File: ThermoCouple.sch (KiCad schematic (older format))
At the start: 0 parts

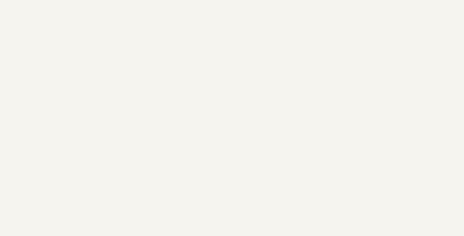
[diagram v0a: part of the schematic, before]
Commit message: create inputs and outputs for main modules
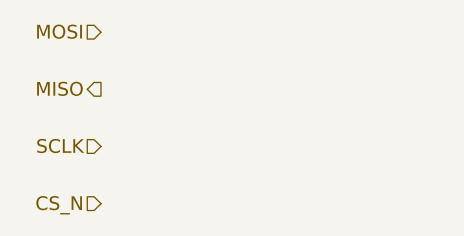
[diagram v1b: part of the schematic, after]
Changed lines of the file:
@@
 Text HLabel 8800 2900 0    60   Input ~ 0
 TC IN -
+Text HLabel 2850 2650 0    60   Input ~ 0
+MOSI
+Text HLabel 2850 2900 0    60   Output ~ 0
+MISO
+Text HLabel 2850 3150 0    60   Input ~ 0
+SCLK
+Text HLabel 2850 3400 0    60   Input ~ 0
+CS_N
 $EndSCHEMATC

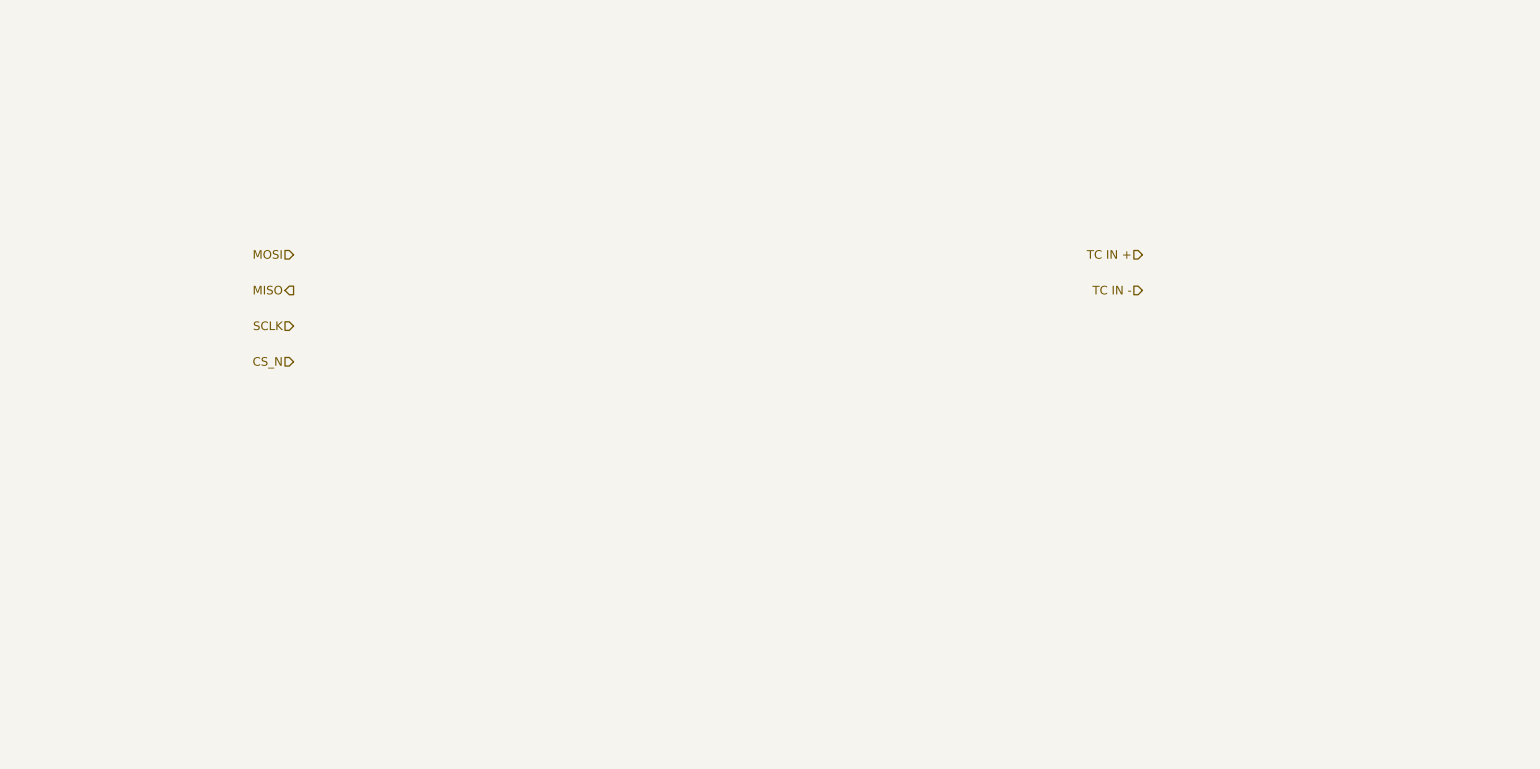
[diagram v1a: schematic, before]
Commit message: Added Start of thermocouple circuit
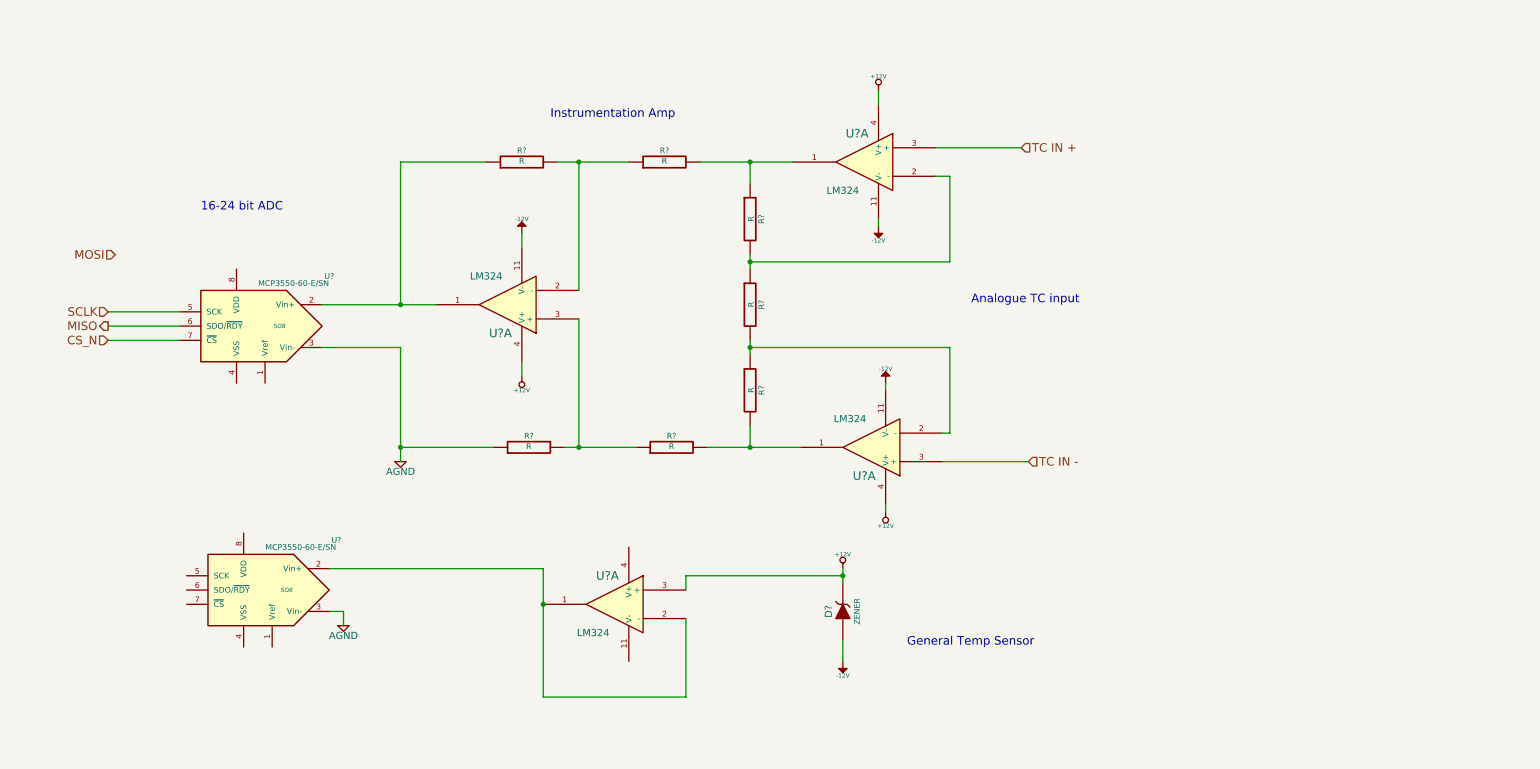
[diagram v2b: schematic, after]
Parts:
- added D?: ZENER, ~, symbol ZENER
- added R? (x7): R, ~, symbol R
- added U? (x4): LM324, symbol LM324
- added U? (x2): MCP3550-60-E/SN, SO8, symbol MCP3550-60-E/SN
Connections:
- net CS_N: now also U?.7 (~CS~)
- net MISO: now also U?.6 (SDO/~RDY~)
- net SCLK: now also U?.5 (SCK)
- net TC IN +: now also U?.3 (+)
- net TC IN -: now also U?.3 (+)
- new net: R?.1, R?.2, U?.1
- new net: R?.1, R?.2, U?.2 (-) (x3)
- new net: R?.2, R?.2, U?.1
- new net: R?.1, U?.1, U?.2 (Vin+)
- new net: R?.1, R?.2, U?.3 (+)
- new net: U?.1, U?.2 (-), U?.2 (Vin+)
- new net +12V: D?.2 (K), U?.3 (+), U?.4 (V+), U?.4 (V+), U?.4 (V+)
- new net -12V: D?.1 (A), U?.11 (V-), U?.11 (V-), U?.11 (V-)
- new net AGND: R?.1, U?.3 (Vin-), U?.3 (Vin-)
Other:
- note added: "16-24 bit ADC"
- note added: "Analogue TC input"
- note added: "General Temp Sensor"
- note added: "Instrumentation Amp"

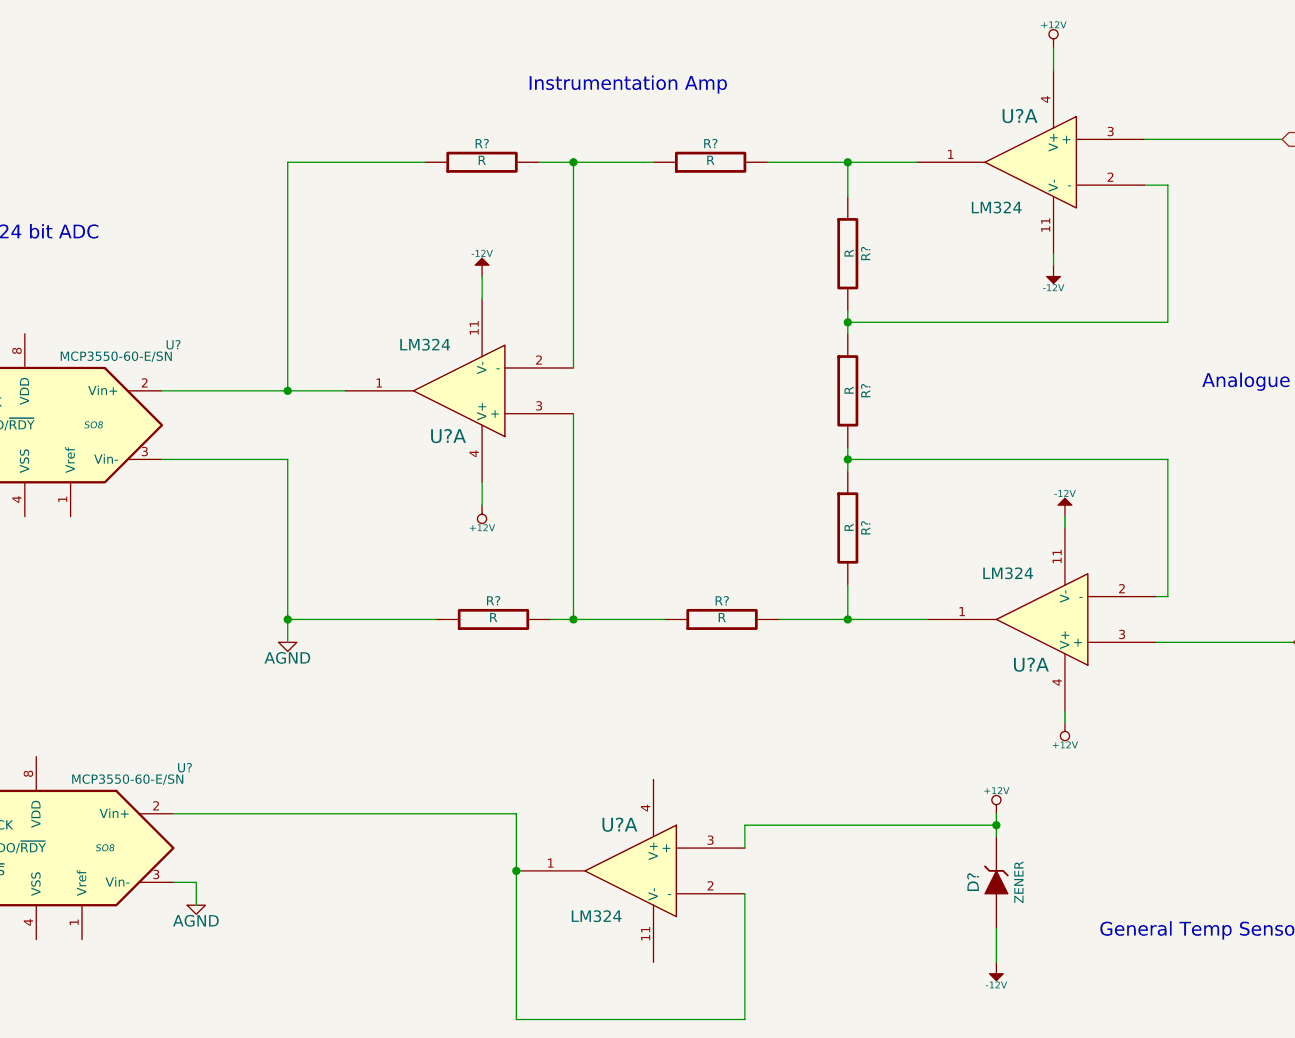
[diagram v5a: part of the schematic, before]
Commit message: Begin Associating relay Module
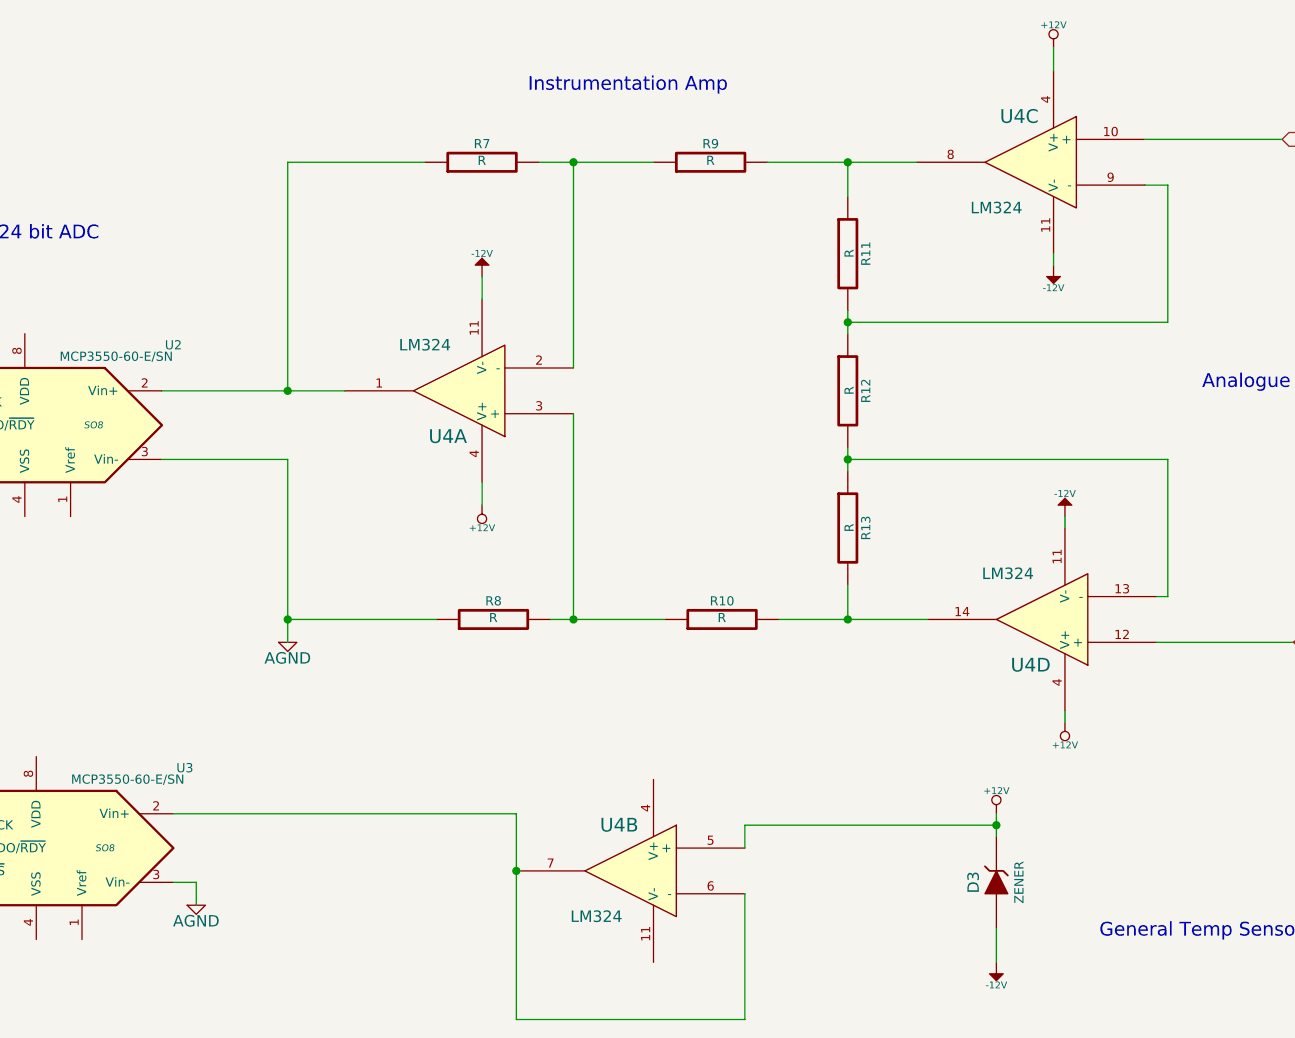
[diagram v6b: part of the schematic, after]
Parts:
- gave numbers to parts that had none: 11
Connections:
- net +12V: now also U4.5 (+); no longer U4.3 (+)
- net TC IN +: now also U4.10 (+); no longer U4.3 (+)
- net TC IN -: now also U4.12 (+); no longer U4.3 (+)
- net at R11.1, R9.2: now also U4.8; no longer U4.1
- net at R11.2, R12.1: now also U4.9 (-); no longer U4.2 (-)
- net at R10.2, R13.2: now also U4.14; no longer U4.1
- net at R12.2, R13.1: now also U4.13 (-); no longer U4.2 (-)
- new net: U3.2 (Vin+), U4.6 (-), U4.7
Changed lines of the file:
@@
 LIBS:BenchBudEE
 LIBS:BenchBudEE-cache
-EELAYER 27 0
+EELAYER 24 0
 EELAYER END
 $Descr A4 11693 8268
@@
 CS_N
 $Comp
-L LM324 U?
-U 1 1 52EF7A2B
+L LM324 U4
+U 3 1 52EF7A2B
 P 6850 2000
-F 0 "U?" H 6900 2200 60  0000 C CNN
+F 0 "U4" H 6900 2200 60  0000 C CNN
 F 1 "LM324" H 7000 1800 50  0000 C CNN
 F 2 "" H 6850 2000 60  0000 C CNN
 F 3 "" H 6850 2000 60  0000 C CNN
-	1    6850 2000
+	3    6850 2000
 	-1   0    0    -1
 $EndComp
 $Comp
-L LM324 U?
-U 1 1 52EF7A3D
+L LM324 U4
+U 4 1 52EF7A3D
 P 6900 4000
-F 0 "U?" H 6950 4200 60  0000 C CNN
+F 0 "U4" H 6950 4200 60  0000 C CNN
 F 1 "LM324" H 7050 3800 50  0000 C CNN
 F 2 "" H 6900 4000 60  0000 C CNN
 F 3 "" H 6900 4000 60  0000 C CNN
-	1    6900 4000
-	-1   0    0    1
-$EndComp
-$Comp
-L LM324 U?
+	4    6900 4000
+	-1   0    0    1
+$EndComp
+$Comp
+L LM324 U4
 U 1 1 52EF7A43
 P 4350 3000
-F 0 "U?" H 4400 3200 60  0000 C CNN
+F 0 "U4" H 4400 3200 60  0000 C CNN
 F 1 "LM324" H 4500 2800 50  0000 C CNN
 F 2 "" H 4350 3000 60  0000 C CNN
@@
 $EndComp
 $Comp
-L LM324 U?
-U 1 1 52EF7A49
+L LM324 U4
+U 2 1 52EF7A49
 P 5100 5100
-F 0 "U?" H 5150 5300 60  0000 C CNN
+F 0 "U4" H 5150 5300 60  0000 C CNN
 F 1 "LM324" H 5250 4900 50  0000 C CNN
 F 2 "" H 5100 5100 60  0000 C CNN
 F 3 "" H 5100 5100 60  0000 C CNN
-	1    5100 5100
+	2    5100 5100
 	-1   0    0    -1
 $EndComp
 $Comp
-L R R?
+L R R11
 U 1 1 52EF7AE3
 P 6050 2400
-F 0 "R?" V 6130 2400 40  0000 C CNN
+F 0 "R11" V 6130 2400 40  0000 C CNN
 F 1 "R" V 6057 2401 40  0000 C CNN
 F 2 "~" V 5980 2400 30  0000 C CNN
@@
 $EndComp
 $Comp
-L R R?
+L R R12
 U 1 1 52EF7AEB
 P 6050 3000
-F 0 "R?" V 6130 3000 40  0000 C CNN
+F 0 "R12" V 6130 3000 40  0000 C CNN
 F 1 "R" V 6057 3001 40  0000 C CNN
 F 2 "~" V 5980 3000 30  0000 C CNN
@@
 $EndComp
 $Comp
-L R R?
+L R R13
 U 1 1 52EF7AF1
 P 6050 3600
-F 0 "R?" V 6130 3600 40  0000 C CNN
+F 0 "R13" V 6130 3600 40  0000 C CNN
 F 1 "R" V 6057 3601 40  0000 C CNN
 F 2 "~" V 5980 3600 30  0000 C CNN
@@
 $EndComp
 $Comp
-L R R?
+L R R9
 U 1 1 52EF7B48
 P 5450 2000
-F 0 "R?" V 5530 2000 40  0000 C CNN
+F 0 "R9" V 5530 2000 40  0000 C CNN
 F 1 "R" V 5457 2001 40  0000 C CNN
 F 2 "~" V 5380 2000 30  0000 C CNN
@@
 $EndComp
 $Comp
-L R R?
+L R R10
 U 1 1 52EF7B50
 P 5500 4000
-F 0 "R?" V 5580 4000 40  0000 C CNN
+F 0 "R10" V 5580 4000 40  0000 C CNN
 F 1 "R" V 5507 4001 40  0000 C CNN
 F 2 "~" V 5430 4000 30  0000 C CNN
@@
 $EndComp
 $Comp
-L R R?
+L R R7
 U 1 1 52EF7B60
 P 4450 2000
-F 0 "R?" V 4530 2000 40  0000 C CNN
+F 0 "R7" V 4530 2000 40  0000 C CNN
 F 1 "R" V 4457 2001 40  0000 C CNN
 F 2 "~" V 4380 2000 30  0000 C CNN
@@
 $EndComp
 $Comp
-L R R?
+L R R8
 U 1 1 52EF7B66
 P 4500 4000
-F 0 "R?" V 4580 4000 40  0000 C CNN
+F 0 "R8" V 4580 4000 40  0000 C CNN
 F 1 "R" V 4507 4001 40  0000 C CNN
 F 2 "~" V 4430 4000 30  0000 C CNN
@@
 $EndComp
 $Comp
-L -12V #PWR?
+L -12V #PWR3
 U 1 1 52EF7E09
 P 4450 2500
-F 0 "#PWR?" H 4450 2630 20  0001 C CNN
+F 0 "#PWR3" H 4450 2630 20  0001 C CNN
 F 1 "-12V" H 4450 2600 30  0000 C CNN
 F 2 "" H 4450 2500 60  0000 C CNN
@@
 $EndComp
 $Comp
-L -12V #PWR?
+L -12V #PWR8
 U 1 1 52EF7E16
 P 6950 2450
-F 0 "#PWR?" H 6950 2580 20  0001 C CNN
+F 0 "#PWR8" H 6950 2580 20  0001 C CNN
 F 1 "-12V" H 6950 2550 30  0000 C CNN
 F 2 "" H 6950 2450 60  0000 C CNN
@@
 $EndComp
 $Comp
-L -12V #PWR?
+L -12V #PWR9
 U 1 1 52EF7E1C
 P 7000 3550
-F 0 "#PWR?" H 7000 3680 20  0001 C CNN
+F 0 "#PWR9" H 7000 3680 20  0001 C CNN
 F 1 "-12V" H 7000 3650 30  0000 C CNN
 F 2 "" H 7000 3550 60  0000 C CNN
@@
 $EndComp
 $Comp
-L +12V #PWR?
+L +12V #PWR4
 U 1 1 52EF7E81
 P 4450 3500
-F 0 "#PWR?" H 4450 3450 20  0001 C CNN
+F 0 "#PWR4" H 4450 3450 20  0001 C CNN
 F 1 "+12V" H 4450 3600 30  0000 C CNN
 F 2 "" H 4450 3500 60  0000 C CNN
@@
 $EndComp
 $Comp
-L +12V #PWR?
+L +12V #PWR10
 U 1 1 52EF7E8E
 P 7000 4450
-F 0 "#PWR?" H 7000 4400 20  0001 C CNN
+F 0 "#PWR10" H 7000 4400 20  0001 C CNN
 F 1 "+12V" H 7000 4550 30  0000 C CNN
 F 2 "" H 7000 4450 60  0000 C CNN
@@
 $EndComp
 $Comp
-L +12V #PWR?
+L +12V #PWR7
 U 1 1 52EF7E9E
 P 6950 1500
-F 0 "#PWR?" H 6950 1450 20  0001 C CNN
+F 0 "#PWR7" H 6950 1450 20  0001 C CNN
 F 1 "+12V" H 6950 1600 30  0000 C CNN
 F 2 "" H 6950 1500 60  0000 C CNN
@@
 $EndComp
 $Comp
-L AGND #PWR?
+L AGND #PWR2
 U 1 1 52EF7F2A
 P 3600 4100
-F 0 "#PWR?" H 3600 4100 40  0001 C CNN
+F 0 "#PWR2" H 3600 4100 40  0001 C CNN
 F 1 "AGND" H 3600 4030 50  0000 C CNN
 F 2 "" H 3600 4100 60  0000 C CNN
@@
 $EndComp
 $Comp
-L MCP3550-60-E/SN U?
+L MCP3550-60-E/SN U2
 U 1 1 52EF80E6
 P 2550 3150
-F 0 "U?" H 2000 3500 40  0000 C CNN
+F 0 "U2" H 2000 3500 40  0000 C CNN
 F 1 "MCP3550-60-E/SN" H 2250 3450 40  0000 C CNN
 F 2 "SO8" H 2350 3150 30  0000 C CIN
@@
 	2050 3050 1550 3050
 $Comp
-L MCP3550-60-E/SN U?
+L MCP3550-60-E/SN U3
 U 1 1 52EF8224
 P 2600 5000
-F 0 "U?" H 2050 5350 40  0000 C CNN
+F 0 "U3" H 2050 5350 40  0000 C CNN
 F 1 "MCP3550-60-E/SN" H 2300 5300 40  0000 C CNN
 F 2 "SO8" H 2400 5000 30  0000 C CIN
@@
 $EndComp
 $Comp
-L ZENER D?
+L ZENER D3
 U 1 1 52EF8236
 P 6700 5150
-F 0 "D?" H 6700 5250 50  0000 C CNN
+F 0 "D3" H 6700 5250 50  0000 C CNN
 F 1 "ZENER" H 6700 5050 40  0000 C CNN
 F 2 "~" H 6700 5150 60  0000 C CNN
@@
 $EndComp
 $Comp
-L +12V #PWR?
+L +12V #PWR5
 U 1 1 52EF824D
 P 6700 4850
-F 0 "#PWR?" H 6700 4800 20  0001 C CNN
+F 0 "#PWR5" H 6700 4800 20  0001 C CNN
 F 1 "+12V" H 6700 4950 30  0000 C CNN
 F 2 "" H 6700 4850 60  0000 C CNN
@@
 $EndComp
 $Comp
-L -12V #PWR?
+L -12V #PWR6
 U 1 1 52EF8253
 P 6700 5500
-F 0 "#PWR?" H 6700 5630 20  0001 C CNN
+F 0 "#PWR6" H 6700 5630 20  0001 C CNN
 F 1 "-12V" H 6700 5600 30  0000 C CNN
 F 2 "" H 6700 5500 60  0000 C CNN
@@
 Connection ~ 4600 5100
 $Comp
-L AGND #PWR?
+L AGND #PWR1
 U 1 1 52EF8398
 P 3200 5250
-F 0 "#PWR?" H 3200 5250 40  0001 C CNN
+F 0 "#PWR1" H 3200 5250 40  0001 C CNN
 F 1 "AGND" H 3200 5180 50  0000 C CNN
 F 2 "" H 3200 5250 60  0000 C CNN
